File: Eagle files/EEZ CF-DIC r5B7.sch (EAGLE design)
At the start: 276 parts, among them IC1 VIPer35L, IC2 SI8233BB-D-IS1, IC3 LM5041B, IC4 LM258D, IC5 IR11688STRPBF, IC6 LM258D, IC7 TL103W, P1 T910W-50K, Q1 MMBT5551, Q10 BC856C, Q2 C3M0280090D, Q3 C3M0280090D, Q4 NYC0102BLT1G, Q5 IRFP4332PBF, Q6 IRFP4332PBF, Q7 FDD86250-F085, Q8 FDD86250-F085, Q9 BC856C, X1 39-30-3035, X2 22-05-7095, X3 B2B-ZR, X4 39-30-1020

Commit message: #7, #8
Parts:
- removed C4A: N.C., EEZ_Lib1:C-EUCY-ROTATED
- removed C5A: N.C., EEZ_Lib1:C-EUCY
- removed Q10, Q9: BC856C, transistor:BC857C-PNP-SOT23-BEC
- removed R100, R98: 39K, rcl:R-EU_R0805
- removed R95, R96: 10K, rcl:R-EU_R0805
- removed R97: 180K, rcl:R-EU_R0805
- removed R99: 18K, rcl:R-EU_R0805
- added F1: 0031.7601, EEZ_Lib1:FUSE_TR5
- added SH4: (no value), EEZ_Lib1:SHORTNOHOLE
- added ZD6: SMAJ58A-TR, EEZ_Lib1:PSMAXX
- C4: value N.C. -> CY1Y-4N7; device rcl:C-EUC0603 -> EEZ_Lib1:C-EUCY-ROTATED
- C49: value 2n2 -> 470p
- C5: value EEEFK1V470P -> N.C.; device EEZ_Lib1:ECAPPANASONIC_H -> rcl:C-EUC0603
- C50: value 100p -> 470p
- C6: value 1u -> EEEFK1V470P; device rcl:C-EUC0805 -> EEZ_Lib1:ECAPPANASONIC_H
- C7: value CY1Y-4N7 -> 1u; device EEZ_Lib1:C-EUCY -> rcl:C-EUC0805
- R32: value 22R/2-3W -> 10R; device rcl:R-EU_R2512 -> rcl:R-EU_R0805
- R33: value 30K -> 22R/2-3W; device rcl:R-EU_R0805 -> rcl:R-EU_R2512
- R34: value 1R -> 30K
- R35: value 10R -> 1R
- R37: value N.C. -> 10R
- R38: value 47K -> N.C.
- R39: value 1R -> 47K
- R40: value 22R/2-3W -> 1R; device rcl:R-EU_R2512 -> rcl:R-EU_R0805
- R41: value 1K -> 22R/2-3W; device rcl:R-EU_R0805 -> rcl:R-EU_R2512
- R42: value N.C. -> 1K; device rcl:R-EU_R2512 -> rcl:R-EU_R0805
- R43: value 10R -> N.C.; device rcl:R-EU_R0805 -> rcl:R-EU_R2512
- R54: value 1K -> 220p
- R57: value 1K -> 7K5
- ZD4: value BZT52C6V2 -> MMSZ5V1T1G
- ZD5: value SMAJ58A-TR -> BZT52C6V2; device EEZ_Lib1:PSMAXX -> EEZ_Lib1:ZENER-DIODESOD123
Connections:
- removed net N$62: Q10.E, R95.2
- removed net N$68: R100.1, R98.2, R99.1
- removed net N$70: Q10.B, R97.2, R98.1
- new net N$74: OK3.EMIT
- net +12V: now also R37.2; no longer R36.2
- net +5VREF: now also R32.1, ZD4.C; no longer R43.1, R95.1, R97.1
- net 0V: now also C5.2, C6.-, C7.2, R40.1, R40.2, SH3.GND_A, ZD4.A; no longer C4.2, C5.-, C6.2, R38.2, R39.1, SH2.GND_A
- net AC_L_IN: now also C8.2; no longer C5A.2
- net AC_N_IN: now also C4.2; no longer C4A.2
- net AGND: now also R35.1, R35.2, SH3.GND_B, ZD5.A; no longer OK3.EMIT, Q9.C, R33.1, R34.2, R96.2, R99.2, ZD4.A
- net AUX_REC: now also C6.+; no longer C5.+
- net CLAMP_C: now also R41.1, R43.1; no longer R40.1, R42.1
- net COMP: now also C49.2, R57.1; no longer C50.2, Q9.E
- net CT_OUT-: now also SH2.GND_A; no longer R57.1
- net GND: now also ZD6.A; no longer ZD5.A
- net LO_OUT: now also R36.1, R38.1; no longer R35.1, R37.1
- net N$130: now also R42.2; no longer R41.2
- net N$133: now also C7.1; no longer C6.1
- net N$17: now also R33.1; no longer R32.1
- net N$24: now also C5.1; no longer C4.1
- net N$25: now also ZD5.C; no longer ZD4.C
- net N$29: now also R36.2, R39.1; no longer R35.2, R38.1
- net N$32: now also R42.1; no longer R41.1
- net N$35: now also R41.2, R43.2; no longer R40.2, R42.2
- net N$37: now also C50.2; no longer C49.2
- net N$41: no longer C8.2
- net N$43: now also F1.1; no longer B1.AC2, C7.2
- net N$48: now also R34.2; no longer R33.2
- net N$5: now also R33.2; no longer R32.2
- net N$52: now also R38.2; no longer R37.2
- net N$61: now also B1.AC2, F1.2; no longer Q10.C, Q9.B, R96.1
- net N$63: now also R37.1; no longer R36.1
- net PE: now also C4.1; no longer C4A.1, C5A.1, C7.1
- net POUT+: now also SH4.GND_B; no longer SH3.GND_B
- net PREG_OUT+: now also ZD6.C; no longer ZD5.C
- net REF: now also R32.2; no longer R43.2
- net S_COMM: now also SH4.GND_A; no longer SH3.GND_A
- net UVLO: no longer R100.2
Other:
- note added: "NFB with Vout tracker"
- note removed: "Active Duty cycle limiter"
- note removed: "NFB with Vout tracker, Duty cycle limiter"
- note removed: "Rshift"
- note removed: "Rslope"
- moved on the sheet: C4, C49, C50, C7, C8, R32, R33, R34, R35, R36, R37, R38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

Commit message: BOM update for #7, #8
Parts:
- R2, R3: value 220K -> 470K
- R54: value 220p -> 220R
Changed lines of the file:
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@@
 <setting verticaltext="up"/>
 </settings>
-<grid distance="0.1" unitdist="inch" unit="inch" style="lines" multiple="1" display="no" altdistance="0.01" altunitdist="inch" altunit="inch"/>
+<grid distance="0.025" unitdist="inch" unit="inch" style="lines" multiple="4" display="no" altdistance="0.01" altunitdist="inch" altunit="inch"/>
 <layers>
 <layer number="1" name="Top" color="4" fill="1" visible="no" active="no"/>
@@
 <part name="C2" library="rcl" deviceset="C-EU" device="150-072X183" value="MKP-X2-220NR15/310"/>
 <part name="C3" library="rcl" deviceset="C-EU" device="150-072X183" value="MKP-X2-220NR15/310"/>
-<part name="R3" library="rcl" deviceset="R-EU_" device="R1206" value="220K"/>
+<part name="R3" library="rcl" deviceset="R-EU_" device="R1206" value="470K"/>
 <part name="X1" library="EEZ_connectors" deviceset="MINIFIT_6659-3" device="-CRE" value="39-30-3035"/>
 <part name="PE1" library="supply1" deviceset="PE" device=""/>
-<part name="R2" library="rcl" deviceset="R-EU_" device="R1206" value="220K"/>
+<part name="R2" library="rcl" deviceset="R-EU_" device="R1206" value="470K"/>
 <part name="SAR2" library="EEZ_Lib1" deviceset="SAR" device="PCB-2.4MM" value="PCB 2.4mm"/>
 <part name="B1" library="EEZ_Lib1" deviceset="BRIDGE" device="-CREEPAGE" value="GBU4K"/>
@@
 <part name="C45" library="rcl" deviceset="C-EU" device="C0603" value="100n"/>
 <part name="D12" library="EEZ_Lib1" deviceset="SCHOTTKY" device="-TO220" value="C3D03060A"/>
-<part name="R54" library="rcl" deviceset="R-EU_" device="R0805" value="220p"/>
+<part name="R54" library="rcl" deviceset="R-EU_" device="R0805" value="220R"/>
 <part name="C50" library="rcl" deviceset="C-EU" device="C0805" value="470p"/>
 <part name="R39" library="rcl" deviceset="R-EU_" device="R0805" value="47K"/>
@@
 <text x="68.58" y="19.05" size="1.27" layer="100">Rfb1</text>
 <rectangle x1="182.88" y1="146.685" x2="187.96" y2="154.305" layer="97"/>
-<rectangle x1="21.59" y1="154.94" x2="28.575" y2="161.29" layer="97"/>
-<rectangle x1="20.32" y1="139.7" x2="26.035" y2="146.05" layer="97"/>
 <circle x="242.57" y="143.51" radius="0.635" width="0.1524" layer="101"/>
 <circle x="242.57" y="146.05" radius="0.635" width="0.1524" layer="101"/>
@@
 <instance part="R54" gate="G$1" x="134.62" y="68.58" smashed="yes" rot="R180">
 <attribute name="NAME" x="132.715" y="70.0786" size="1.778" layer="95"/>
-<attribute name="VALUE" x="133.35" y="65.278" size="1.778" layer="96"/>
+<attribute name="VALUE" x="132.08" y="65.278" size="1.778" layer="96"/>
 </instance>
 <instance part="C50" gate="G$1" x="127" y="60.96" smashed="yes" rot="R180">

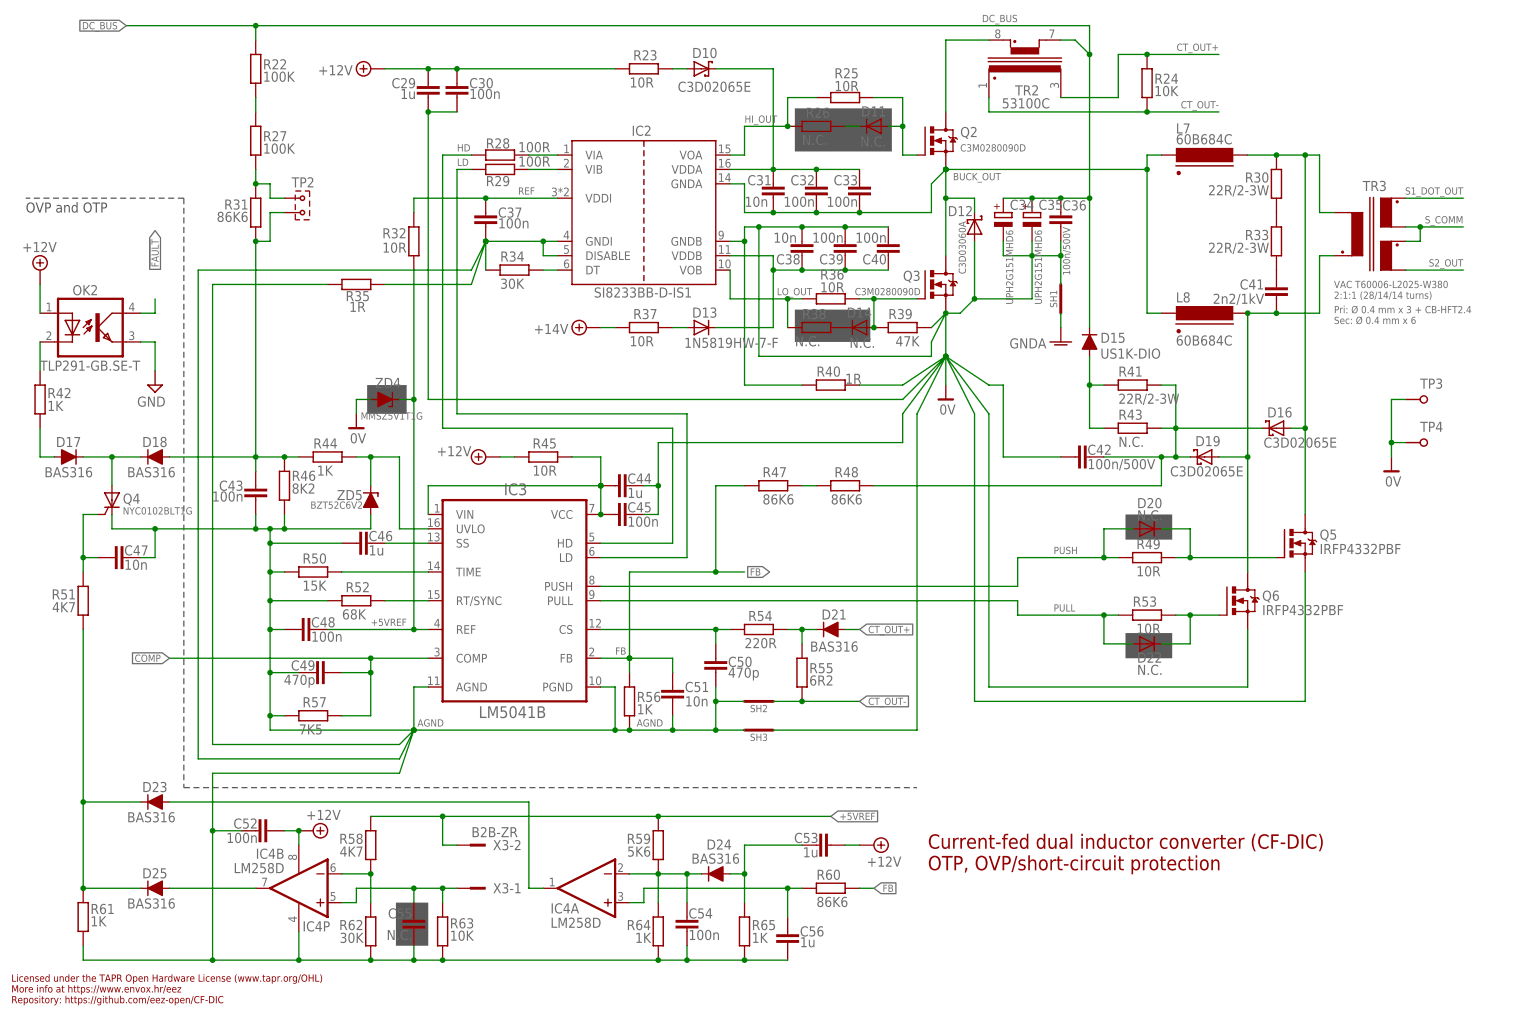
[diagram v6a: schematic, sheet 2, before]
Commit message: new LED1 and primary side snubbers
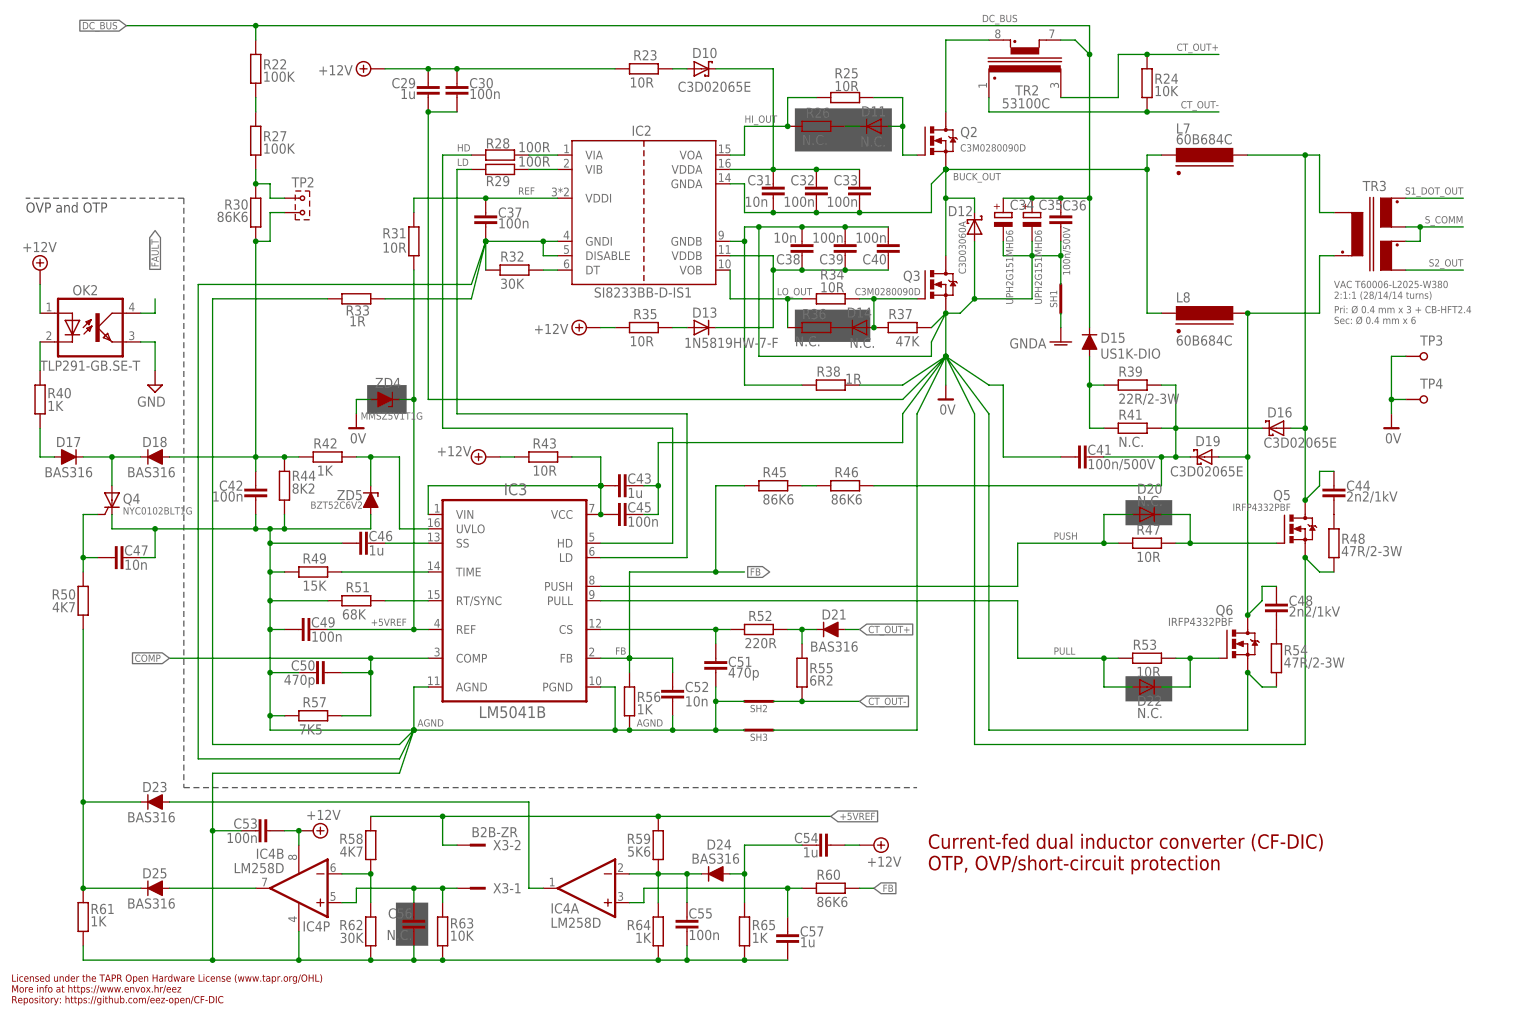
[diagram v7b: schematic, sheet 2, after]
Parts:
- added C82: N.C., rcl:C-EUC0805
- C4: device EEZ_Lib1:C-EUCY-ROTATED -> EEZ_Lib1:C-EUCY
- C41: value 2n2/1kV -> 100n/500V; device rcl:C-EUC1210 -> rcl:C-EUC1812
- C42: value 100n/500V -> 100n; device rcl:C-EUC1812 -> rcl:C-EUC0603
- C43, C54: value 100n -> 1u; device rcl:C-EUC0603 -> rcl:C-EUC0805
- C44: value 1u -> 2n2/1kV; device rcl:C-EUC0805 -> rcl:C-EUC1210
- C48: value 100n -> 2n2/1kV; device rcl:C-EUC0603 -> rcl:C-EUC1210
- C49: value 470p -> 100n; device rcl:C-EUC0805 -> rcl:C-EUC0603
- C51: value 10n -> 470p; device rcl:C-EUC0603 -> rcl:C-EUC0805
- C52: value 100n -> 10n
- C53: value 1u -> 100n; device rcl:C-EUC0805 -> rcl:C-EUC0603
- C55: value N.C. -> 100n
- C56: value 1u -> N.C.; device rcl:C-EUC0805 -> rcl:C-EUC0603
- C57: value UVZ1J222MHD -> 1u; device EEZ_Lib1:ECAPH35.5A -> rcl:C-EUC0805
- C58: value 1u/100V -> UVZ1J222MHD; device rcl:C-EUC1206 -> EEZ_Lib1:ECAPH35.5A
- C59: value 47p/200V -> 1u/100V; device rcl:C-EUC0805 -> rcl:C-EUC1206
- C60: value HHXC630ARA330MHA0G -> 47p/200V; device EEZ_Lib1:ECAPSMD8.3MM/HA0 -> rcl:C-EUC0805
- C61: value 1u/100V -> HHXC630ARA330MHA0G; device rcl:C-EUC1206 -> EEZ_Lib1:ECAPSMD8.3MM/HA0
- C62: value 100n/100V -> 1u/100V
- C63, C70: value 2n2/1kV -> 100n/100V; device rcl:C-EUC1210 -> rcl:C-EUC1206
- C64: value N.C. -> 2n2/1kV; device rcl:C-EUC1206 -> rcl:C-EUC1210
- C65: value 100n -> N.C.; device rcl:C-EUC0603 -> rcl:C-EUC1206
- C66: value 4u7 -> 100n; device rcl:C-EUC1206 -> rcl:C-EUC0603
- C67: value 4n7/200V -> 4u7
- C68: value 4n7/200V -> N.C.
- C69: value 4n7/200V -> 100n/100V
- C71: value 47p/200V -> 2n2/1kV; device rcl:C-EUC0805 -> rcl:C-EUC1210
- C72, C76: value 100n -> 47p/200V; device rcl:C-EUC0603 -> rcl:C-EUC0805
- C73: value 2n2 -> 100n; device rcl:C-EUC0805 -> rcl:C-EUC0603
- C74: value 100n -> 4n7; device rcl:C-EUC0603 -> rcl:C-EUC0805
- C75: value 47p/200V -> 100n; device rcl:C-EUC0805 -> rcl:C-EUC0603
- C77: value 100p -> 100n; device rcl:C-EUC0805 -> rcl:C-EUC0603
- C78: value 1n -> 100p
- C79: value N.C. -> 1n; device EEZ_Lib1:ECAP1206 -> rcl:C-EUC0805
- C80: value 1u -> N.C.; device rcl:C-EUC0805 -> EEZ_Lib1:ECAP1206
- C81: value N.C. -> 1u
- JP2: value JP2-NOCUT -> JP2-CUT; device EEZ_Lib1:JP2-NOCUT -> EEZ_Lib1:JP2-CUT
- LED1: value L-934EB/1Y1ID-RV -> WP934MD/LYLID; device EEZ_Lib1:LED_L-934EB/1Y1ID-RV -> EEZ_Lib1:WP934MD/LYLID
- R30: value 22R/2-3W -> 86K6; device rcl:R-EU_R2512 -> rcl:R-EU_R0805
- R31, R47: value 86K6 -> 10R
- R32: value 10R -> 30K
- R33: value 22R/2-3W -> 1R; device rcl:R-EU_R2512 -> rcl:R-EU_R0805
- R34: value 30K -> 10R
- R35: value 1R -> 10R
- R36: value 10R -> N.C.
- R37: value 10R -> 47K
- R38: value N.C. -> 1R
- R39: value 47K -> 22R/2-3W; device rcl:R-EU_R0805 -> rcl:R-EU_R2512
- R40: value 1R -> 1K
- R41: value 22R/2-3W -> N.C.
- R43: value N.C. -> 10R; device rcl:R-EU_R2512 -> rcl:R-EU_R0805
- R44: value 1K -> 8K2
- R45: value 10R -> 86K6
- R46: value 8K2 -> 86K6
- R48: value 86K6 -> 47R/2-3W; device rcl:R-EU_R0805 -> rcl:R-EU_R2512
- R49: value 10R -> 15K
- R50: value 15K -> 4K7
- R51: value 4K7 -> 68K
- R52: value 68K -> 220R
- R54: value 220R -> 47R/2-3W; device rcl:R-EU_R0805 -> rcl:R-EU_R2512
- R83: value 4K7 -> 1K
- R86: value 27K -> 86K6
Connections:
- removed net N$17: C41.1, R33.1
- removed net N$74: OK3.EMIT
- new net N$68: C44.1, R48.1
- net +12V: now also C54.1, R35.2, R43.2; no longer C52.1, R37.2, R45.2
- net +2.5VREF: now also C81.1; no longer C80.1
- net +5VREF: now also C49.2, R31.1; no longer C48.2, R32.1
- net 0V: now also C41.1, C43.2, JP5.NC, R37.2, R38.1, R38.2, R48.2, R54.2; no longer C42.1, C44.2, JP5.NO, R39.2, R40.1, R40.2
- net AGND: now also C42.2, C51.1, C53.2, C55.2, C57.1, OK3.EMIT, R32.1, R33.1, R33.2, R44.2, R49.2, R51.2; no longer C43.2, C48.1, C51.2, C54.2, C55.1, R34.1, R35.1, R35.2, R46.2, R50.2, R52.2
- net CLAMP_C: now also C41.2, R39.1, R46.2; no longer C42.2, R43.1, R48.2
- net COMP: now also C50.2; no longer C49.2
- net FB: now also C52.1, R45.1; no longer C51.1, R47.1
- net GND: now also C58.-, C59.2, C60.1, C61.-, C64.2, C65.1, C67.2, C70.1, C71.2, C72.1, C73.2, C75.2, C77.2, C80.-, C82.2; no longer C57.-, C58.2, C59.1, C60.-, C61.2, C64.1, C65.2, C69.1, C70.2, C71.1, C72.2, C74.2, C76.2, C79.-, C80.2
- net LO_OUT: now also R34.1; no longer R38.1
- net L_PULL: now also C48.2; no longer C41.2
- net L_PUSH: now also C44.2; no longer R30.2
- net N$10: now also C76.2; no longer C75.2
- net N$100: now also R50.1; no longer R51.1
- net N$13: now also R47.1; no longer R49.1
- net N$130: now also R40.2; no longer R42.2
- net N$134: now also C78.1; no longer C77.1
- net N$19: now also R51.1; no longer R52.1
- net N$2: now also R30.1; no longer R31.1
- net N$22: now also R49.1; no longer R50.1
- net N$25: now also R42.1; no longer R44.1
- net N$28: now also C74.2; no longer C73.2
- net N$29: now also R34.2, R37.1; no longer R36.2, R39.1
- net N$30: now also R45.2, R46.1; no longer R47.2, R48.1
- net N$32: now also R40.1; no longer R42.1
- net N$34: now also C57.2; no longer C56.2
- net N$35: now also R39.2; no longer R43.2
- net N$37: now also C51.2, R52.2; no longer C50.2, R54.2
- net N$39: now also C77.1; no longer C76.1
- net N$42: now also C56.2; no longer C55.2
- net N$46: now also C73.1, C75.1; no longer C72.1, C74.1
- net N$48: now also R32.2; no longer R34.2
- net N$5: now also C48.1, R54.1; no longer R30.1, R33.2
- net N$51: now also R50.2; no longer R51.2
- net N$52: now also R36.2; no longer R38.2
- net N$54: now also C43.1, R43.1; no longer C44.1, R45.1
- net N$56: now also R52.1; no longer R54.1
- net N$57: now also C82.1; no longer C81.1
- net N$59: now also C54.2; no longer C53.2
- net N$63: now also R35.1; no longer R37.1
- net N$64: now also C78.2; no longer C77.2
- net N$66: now also C71.1; no longer C70.1
- net N$67: now also C64.1; no longer C63.1
- net N$7: now also C55.1; no longer C54.1
- net N$71: now also C74.1; no longer C73.1
- net N$76: now also C76.1, C79.1; no longer C75.1, C78.1
- net N$8: now also C65.2; no longer C64.2
- net N$9: now also C79.2; no longer C78.2
- net NFB_OFFSET: now also C80.+; no longer C79.+
- net PE: now also C70.2, JP5.NO; no longer C67.2, JP5.NC
- net POUT+: now also C58.+, C59.1, C68.1; no longer C57.+, C58.1, C67.1
- net PREG_OUT+: now also C61.+, C63.1, C69.1; no longer C60.+, C61.1, C68.1
- net PUSH: now also R47.2; no longer R49.2
- net REF: now also R31.2; no longer R32.2
- net SYNC_VCC: now also C67.1; no longer C65.1
- net UVLO: now also C42.1, R30.2, R42.2, R44.1; no longer C43.1, R31.2, R44.2, R46.1
- net VD1: now also C60.2; no longer C59.2
- net VD2: now also C72.2; no longer C71.2
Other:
- moved on the sheet: C41, C42, C43, C44, C48, C49, C50, C51, C52, C53, C54, C55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
